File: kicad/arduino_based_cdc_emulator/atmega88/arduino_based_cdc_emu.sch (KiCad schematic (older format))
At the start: 12 parts, among them IC1 ATMEGA88-A, P1 CONN_5, U1 78L05, X1 20MHz

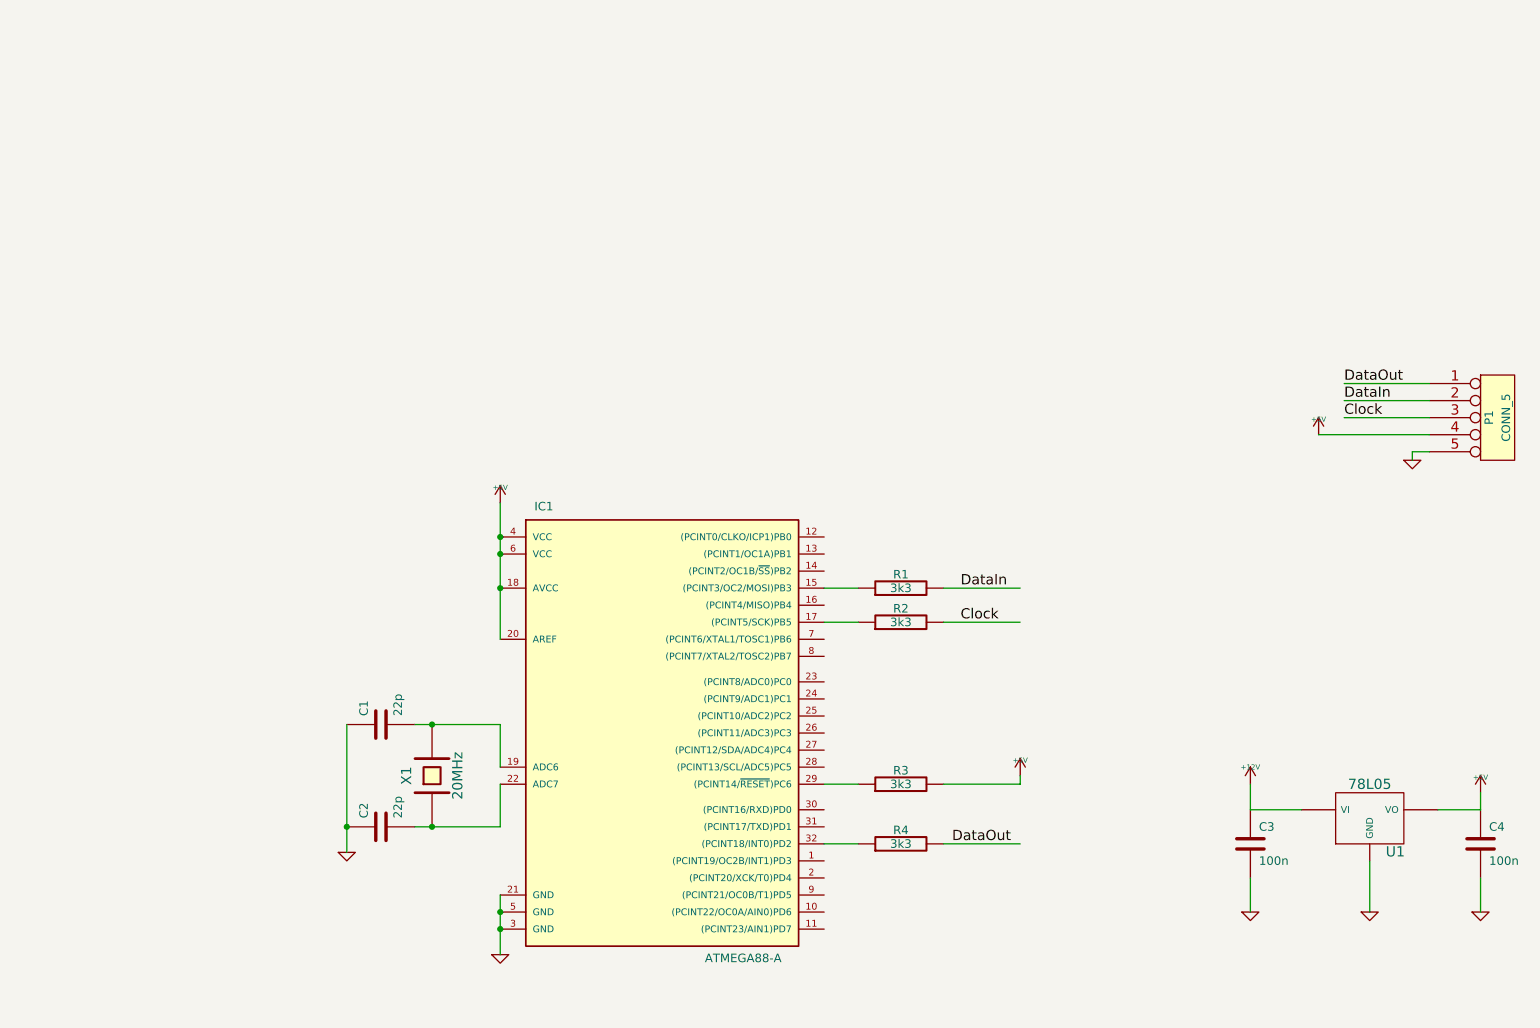
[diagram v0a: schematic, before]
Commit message: arduino based cdc emulator pcb
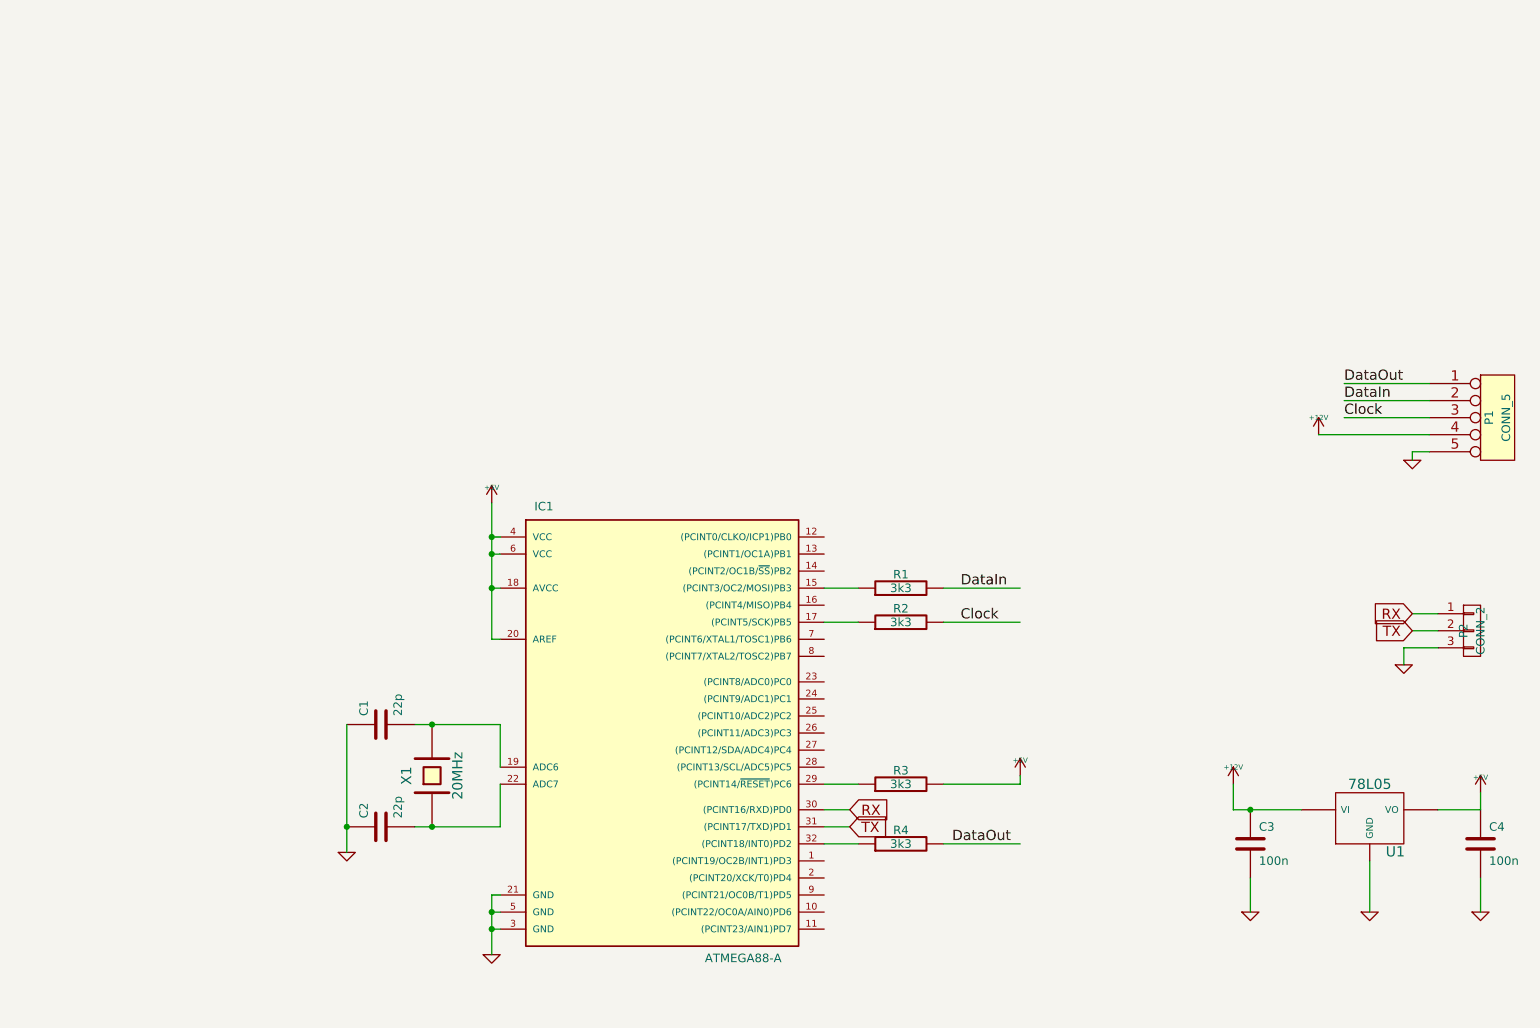
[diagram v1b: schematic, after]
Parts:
- added P2: CONN_2, symbol CONN_01X03
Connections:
- net labels added: RX, TX
- wire segments 29 -> 42
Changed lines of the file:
@@
-EESchema Schematic File Version 2  date Wed 12 Mar 2014 03:47:41 PM CET
+EESchema Schematic File Version 2
 LIBS:power
 LIBS:device
@@
 LIBS:valves
 LIBS:arduino_based_cdc_emu-cache
-EELAYER 25  0
+EELAYER 25 0
 EELAYER END
-$Descr A4 11700 8267
+$Descr A4 11693 8268
 encoding utf-8
 Sheet 1 1
@@
 	10000 5350 10000 5450
 Wire Wire Line
-	10000 5450 9750 5450
-Wire Wire Line
 	10000 5850 10000 6050
 Wire Wire Line
@@
 Wire Wire Line
 	6350 4150 6150 4150
-Connection ~ 4250 4150
-Wire Wire Line
-	4250 4450 4250 3650
-Connection ~ 4250 3850
-Connection ~ 4250 6050
-Wire Wire Line
-	4250 5950 4250 6300
 Wire Wire Line
 	4250 5300 4250 5550
@@
 	3350 5700 3350 4950
 Connection ~ 3350 5550
-Connection ~ 4250 6150
-Connection ~ 4250 3950
 Wire Wire Line
 	6350 5650 6150 5650
@@
 	8650 5850 8650 6050
 Wire Wire Line
-	8950 5450 8650 5450
+	8550 5450 8950 5450
 Wire Wire Line
 	9350 5750 9350 6050
-Wire Wire Line
-	8650 5450 8650 5300
 Wire Wire Line
 	9700 3150 9200 3150
@@
 F 0 "#PWR01" H 7300 5340 20  0001 C CNN
 F 1 "+5V" H 7300 5340 30  0000 C CNN
+F 2 "" H 7300 5250 60  0001 C CNN
+F 3 "" H 7300 5250 60  0001 C CNN
 	1    7300 5250
 	1    0    0    -1
@@
 F 0 "R3" V 6680 5300 50  0000 C CNN
 F 1 "3k3" V 6600 5300 50  0000 C CNN
+F 2 "" H 6600 5300 60  0001 C CNN
+F 3 "" H 6600 5300 60  0001 C CNN
 	1    6600 5300
 	0    -1   -1   0
@@
 DataOut
 $Comp
-L +5V #PWR02
-U 1 1 530C9464
-P 9050 3250
-F 0 "#PWR02" H 9050 3340 20  0001 C CNN
-F 1 "+5V" H 9050 3340 30  0000 C CNN
-	1    9050 3250
-	1    0    0    -1
-$EndComp
-$Comp
-L GND #PWR03
+L GND #PWR02
 U 1 1 530C945D
 P 9600 3400
-F 0 "#PWR03" H 9600 3400 30  0001 C CNN
+F 0 "#PWR02" H 9600 3400 30  0001 C CNN
 F 1 "GND" H 9600 3330 30  0001 C CNN
+F 2 "" H 9600 3400 60  0001 C CNN
+F 3 "" H 9600 3400 60  0001 C CNN
 	1    9600 3400
 	1    0    0    -1
@@
 F 0 "P1" V 10050 3150 50  0000 C CNN
 F 1 "CONN_5" V 10150 3150 50  0000 C CNN
+F 2 "" H 10100 3150 60  0001 C CNN
+F 3 "" H 10100 3150 60  0001 C CNN
 	1    10100 3150
 	1    0    0    -1
 $EndComp
 $Comp
-L +12V #PWR04
+L +12V #PWR03
 U 1 1 530C8041
-P 8650 5300
-F 0 "#PWR04" H 8650 5250 20  0001 C CNN
-F 1 "+12V" H 8650 5400 30  0000 C CNN
-	1    8650 5300
-	1    0    0    -1
-$EndComp
-$Comp
-L +5V #PWR05
+P 8550 5300
+F 0 "#PWR03" H 8550 5250 20  0001 C CNN
+F 1 "+12V" H 8550 5400 30  0000 C CNN
+F 2 "" H 8550 5300 60  0001 C CNN
+F 3 "" H 8550 5300 60  0001 C CNN
+	1    8550 5300
+	1    0    0    -1
+$EndComp
+$Comp
+L +5V #PWR04
 U 1 1 530C8014
 P 10000 5350
-F 0 "#PWR05" H 10000 5440 20  0001 C CNN
+F 0 "#PWR04" H 10000 5440 20  0001 C CNN
 F 1 "+5V" H 10000 5440 30  0000 C CNN
+F 2 "" H 10000 5350 60  0001 C CNN
+F 3 "" H 10000 5350 60  0001 C CNN
 	1    10000 5350
 	1    0    0    -1
 $EndComp
 $Comp
-L GND #PWR06
+L GND #PWR05
 U 1 1 530C800A
 P 9350 6050
-F 0 "#PWR06" H 9350 6050 30  0001 C CNN
+F 0 "#PWR05" H 9350 6050 30  0001 C CNN
 F 1 "GND" H 9350 5980 30  0001 C CNN
+F 2 "" H 9350 6050 60  0001 C CNN
+F 3 "" H 9350 6050 60  0001 C CNN
 	1    9350 6050
 	1    0    0    -1
@@
 F 0 "U1" H 9500 5304 60  0000 C CNN
 F 1 "78L05" H 9350 5700 60  0000 C CNN
+F 2 "" H 9350 5500 60  0001 C CNN
+F 3 "" H 9350 5500 60  0001 C CNN
 	1    9350 5500
 	1    0    0    -1
 $EndComp
 $Comp
-L GND #PWR07
+L GND #PWR06
 U 1 1 530C7FEB
 P 10000 6050
-F 0 "#PWR07" H 10000 6050 30  0001 C CNN
+F 0 "#PWR06" H 10000 6050 30  0001 C CNN
 F 1 "GND" H 10000 5980 30  0001 C CNN
+F 2 "" H 10000 6050 60  0001 C CNN
+F 3 "" H 10000 6050 60  0001 C CNN
 	1    10000 6050
 	1    0    0    -1
 $EndComp
 $Comp
-L GND #PWR08
+L GND #PWR07
 U 1 1 530C7FE7
 P 8650 6050
-F 0 "#PWR08" H 8650 6050 30  0001 C CNN
+F 0 "#PWR07" H 8650 6050 30  0001 C CNN
 F 1 "GND" H 8650 5980 30  0001 C CNN
+F 2 "" H 8650 6050 60  0001 C CNN
+F 3 "" H 8650 6050 60  0001 C CNN
 	1    8650 6050
 	1    0    0    -1
@@
 F 0 "C4" H 10050 5750 50  0000 L CNN
 F 1 "100n" H 10050 5550 50  0000 L CNN
+F 2 "" H 10000 5650 60  0001 C CNN
+F 3 "" H 10000 5650 60  0001 C CNN
 	1    10000 5650
 	1    0    0    -1
@@
 F 0 "C3" H 8700 5750 50  0000 L CNN
 F 1 "100n" H 8700 5550 50  0000 L CNN
+F 2 "" H 8650 5650 60  0001 C CNN
+F 3 "" H 8650 5650 60  0001 C CNN
 	1    8650 5650
 	1    0    0    -1
@@
 F 0 "R2" V 6680 4350 50  0000 C CNN
 F 1 "3k3" V 6600 4350 50  0000 C CNN
+F 2 "" H 6600 4350 60  0001 C CNN
+F 3 "" H 6600 4350 60  0001 C CNN
 	1    6600 4350
 	0    -1   -1   0
@@
 F 0 "R1" V 6680 4150 50  0000 C CNN
 F 1 "3k3" V 6600 4150 50  0000 C CNN
+F 2 "" H 6600 4150 60  0001 C CNN
+F 3 "" H 6600 4150 60  0001 C CNN
 	1    6600 4150
 	0    -1   -1   0
@@
 F 0 "R4" V 6680 5650 50  0000 C CNN
 F 1 "3k3" V 6600 5650 50  0000 C CNN
+F 2 "" H 6600 5650 60  0001 C CNN
+F 3 "" H 6600 5650 60  0001 C CNN
 	1    6600 5650
 	0    -1   -1   0
 $EndComp
 $Comp
-L +5V #PWR09
+L +5V #PWR08
 U 1 1 530C77C0
-P 4250 3650
-F 0 "#PWR09" H 4250 3740 20  0001 C CNN
-F 1 "+5V" H 4250 3740 30  0000 C CNN
-	1    4250 3650
+P 4200 3650
+F 0 "#PWR08" H 4200 3740 20  0001 C CNN
+F 1 "+5V" H 4200 3740 30  0000 C CNN
+F 2 "" H 4200 3650 60  0001 C CNN
+F 3 "" H 4200 3650 60  0001 C CNN
+	1    4200 3650
+	1    0    0    -1
+$EndComp
+$Comp
+L GND #PWR09
+U 1 1 530C77A6
+P 4200 6300
+F 0 "#PWR09" H 4200 6300 30  0001 C CNN
+F 1 "GND" H 4200 6230 30  0001 C CNN
+F 2 "" H 4200 6300 60  0001 C CNN
+F 3 "" H 4200 6300 60  0001 C CNN
+	1    4200 6300
 	1    0    0    -1
 $EndComp
 $Comp
 L GND #PWR010
-U 1 1 530C77A6
-P 4250 6300
-F 0 "#PWR010" H 4250 6300 30  0001 C CNN
-F 1 "GND" H 4250 6230 30  0001 C CNN
-	1    4250 6300
-	1    0    0    -1
-$EndComp
-$Comp
-L GND #PWR011
 U 1 1 530C7791
 P 3350 5700
-F 0 "#PWR011" H 3350 5700 30  0001 C CNN
+F 0 "#PWR010" H 3350 5700 30  0001 C CNN
 F 1 "GND" H 3350 5630 30  0001 C CNN
+F 2 "" H 3350 5700 60  0001 C CNN
+F 3 "" H 3350 5700 60  0001 C CNN
 	1    3350 5700
 	1    0    0    -1
@@
 F 0 "C2" H 3600 5650 50  0000 L CNN
 F 1 "22p" H 3600 5450 50  0000 L CNN
+F 2 "" H 3550 5550 60  0001 C CNN
+F 3 "" H 3550 5550 60  0001 C CNN
 	1    3550 5550
 	0    -1   -1   0
@@
 F 0 "C1" H 3600 5050 50  0000 L CNN
 F 1 "22p" H 3600 4850 50  0000 L CNN
+F 2 "" H 3550 4950 60  0001 C CNN
+F 3 "" H 3550 4950 60  0001 C CNN
 	1    3550 4950
 	0    -1   -1   0
@@
 F 0 "X1" H 3850 5400 60  0000 C CNN
 F 1 "20MHz" H 3850 5100 60  0000 C CNN
+F 2 "" H 3850 5250 60  0001 C CNN
+F 3 "" H 3850 5250 60  0001 C CNN
 	1    3850 5250
 	0    -1   -1   0
@@
 F 1 "ATMEGA88-A" H 5450 3550 50  0000 L BNN
 F 2 "TQFP32" H 4600 3600 50  0001 C CNN
+F 3 "" H 5150 4950 60  0001 C CNN
 	1    5150 4950
 	1    0    0    -1
 $EndComp
+$Comp
+L +12V #PWR011
+U 1 1 543549B8
+P 9050 3250
+F 0 "#PWR011" H 9050 3200 20  0001 C CNN
+F 1 "+12V" H 9050 3350 30  0000 C CNN
+F 2 "" H 9050 3250 60  0001 C CNN
+F 3 "" H 9050 3250 60  0001 C CNN
+	1    9050 3250
+	1    0    0    -1
+$EndComp
+Wire Wire Line
+	4250 4450 4200 4450
+Wire Wire Line
+	4200 4450 4200 3650
+Wire Wire Line
+	4250 4150 4200 4150
+Connection ~ 4200 4150
+Wire Wire Line
+	4250 3950 4200 3950
+Connection ~ 4200 3950
+Wire Wire Line
+	4250 3850 4200 3850
+Connection ~ 4200 3850
+Wire Wire Line
+	4250 5950 4200 5950
+Wire Wire Line
+	4200 5950 4200 6300
+Wire Wire Line
+	4250 6050 4200 6050
+Connection ~ 4200 6050
+Wire Wire Line
+	4250 6150 4200 6150
+Connection ~ 4200 6150
+Wire Wire Line
+	8550 5450 8550 5300
+Connection ~ 8650 5450
+Wire Wire Line
+	10000 5450 9750 5450
+$Comp
+L CONN_01X03 P2
+U 1 1 54357812
+P 9950 4400
+F 0 "P2" V 9900 4400 50  0000 C CNN
+F 1 "CONN_2" V 10000 4400 50  0000 C CNN
+F 2 "" H 9950 4400 60  0001 C CNN
+F 3 "" H 9950 4400 60  0001 C CNN
+	1    9950 4400
+	1    0    0    -1
+$EndComp
+Text GLabel 9600 4300 0    60   Input ~ 0
+RX
+Text GLabel 6300 5450 2    60   Input ~ 0
+RX
+Wire Wire Line
+	6300 5450 6150 5450
+Wire Wire Line
+	6150 5550 6300 5550
+Text GLabel 6300 5550 2    60   Input ~ 0
+TX
+Text GLabel 9600 4400 0    60   Input ~ 0
+TX
+Wire Wire Line
+	9600 4300 9750 4300
+Wire Wire Line
+	9600 4400 9750 4400
+$Comp
+L GND #PWR012
+U 1 1 54358932
+P 9550 4600
+F 0 "#PWR012" H 9550 4600 30  0001 C CNN
+F 1 "GND" H 9550 4530 30  0001 C CNN
+F 2 "" H 9550 4600 60  0001 C CNN
+F 3 "" H 9550 4600 60  0001 C CNN
+	1    9550 4600
+	1    0    0    -1
+$EndComp
+Wire Wire Line
+	9550 4600 9550 4500
+Wire Wire Line
+	9550 4500 9750 4500
 $EndSCHEMATC

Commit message: same changes
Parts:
- added P3: CONN_3, Pin_Headers:Pin_Header_Straight_1x01, symbol CONN_01X01
- C1, C2, C3, C4: footprint (none) -> Capacitors_SMD:C_1206_HandSoldering; symbol C -> C-RESCUE-arduino_based_cdc_emu
- IC1: footprint TQFP32 -> SMD_Packages:TQFP-32
- P1: value CONN_5 -> CONN_1; footprint (none) -> Pin_Headers:Pin_Header_Straight_1x05
- P2: footprint (none) -> Pin_Headers:Pin_Header_Straight_1x05; symbol CONN_01X03 -> CONN_01X05
- R1, R2, R3, R4: footprint (none) -> Resistors_SMD:R_1206_HandSoldering; symbol R -> R-RESCUE-arduino_based_cdc_emu
- U1: footprint (none) -> my_modules:SOT-223-REGULATOR
- X1: footprint (none) -> Crystals_Oscillators_SMD:Q_49U3HMS
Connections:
- net labels added: MISO, RESET
- wire segments 42 -> 51
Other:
- moved on the sheet: C1, C2, X1

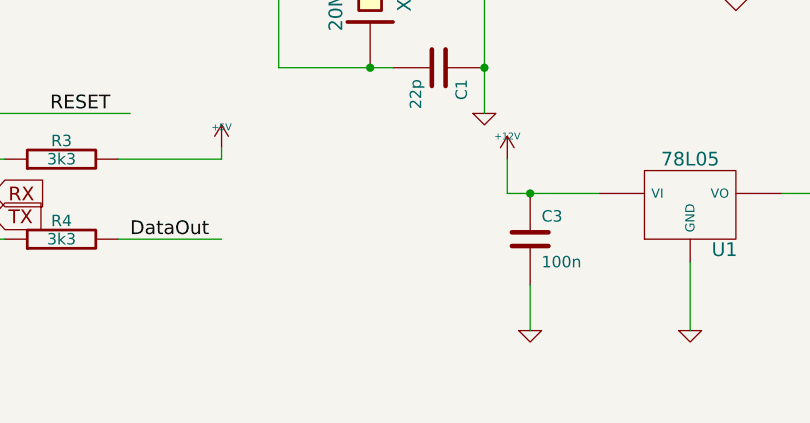
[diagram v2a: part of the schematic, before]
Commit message: pcb, really need rework.
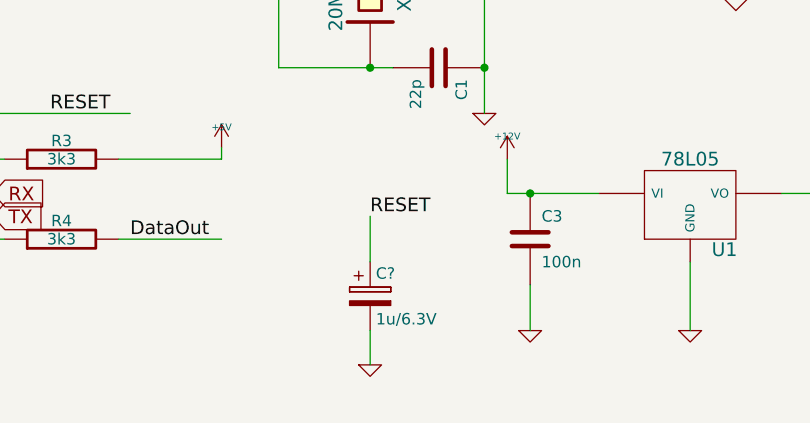
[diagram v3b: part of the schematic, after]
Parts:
- added C?: 1u/6.3V, symbol CP
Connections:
- wire segments 51 -> 53
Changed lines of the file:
@@
 Text Label 6150 3300 0    60   ~ 0
 MISO
+$Comp
+L CP C?
+U 1 1 560D753D
+P 7950 5900
+F 0 "C?" H 7975 6000 50  0000 L CNN
+F 1 "1u/6.3V" H 7975 5800 50  0000 L CNN
+F 2 "" H 7988 5750 30  0000 C CNN
+F 3 "" H 7950 5900 60  0000 C CNN
+	1    7950 5900
+	1    0    0    -1
+$EndComp
+Text Label 7950 5550 0    60   ~ 0
+RESET
+Wire Wire Line
+	7950 5550 7950 5750
+$Comp
+L GND-RESCUE-arduino_based_cdc_emu #PWR?
+U 1 1 560D79D0
+P 7950 6200
+F 0 "#PWR?" H 7950 6200 30  0001 C CNN
+F 1 "GND" H 7950 6130 30  0001 C CNN
+F 2 "" H 7950 6200 60  0001 C CNN
+F 3 "" H 7950 6200 60  0001 C CNN
+	1    7950 6200
+	1    0    0    -1
+$EndComp
+Wire Wire Line
+	7950 6050 7950 6200
 $EndSCHEMATC

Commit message: update
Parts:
- added D1, D2: 1N4148, Diodes_SMD:DO-214AA, symbol D
- added Q1, Q2, Q3: Q_NPN_EBC, symbol Q_NPN_BEC
- added R5, R7, R9: 3k3, Resistors_SMD:R_0805_HandSoldering, symbol R-RESCUE-arduino_based_cdc_emu
- added R6, R8: 47k, Resistors_SMD:R_0805_HandSoldering, symbol R-RESCUE-arduino_based_cdc_emu
- C1, C2: footprint Capacitors_SMD:C_1206_HandSoldering -> Capacitors_SMD:C_0805
- C3, C4: footprint Capacitors_SMD:C_1206_HandSoldering -> Capacitors_SMD:C_0805_HandSoldering
- R1, R2, R4: footprint Resistors_SMD:R_1206_HandSoldering -> Resistors_SMD:R_0805
- R3: footprint Resistors_SMD:R_1206_HandSoldering -> Resistors_SMD:R_0805_HandSoldering
- X1: value 20MHz -> 16MHz
- gave numbers to parts that had none: 1
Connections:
- wire segments 53 -> 71
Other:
- moved on the sheet: C1, C2, C3, C4, C5, IC1, P1, P2, P3, R1, R2, R3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
